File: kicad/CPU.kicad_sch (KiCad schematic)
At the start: 0 parts

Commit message: [kicad] Added HSE + HSE calculation
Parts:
- added C10, C11: 5pF, symbol Device:C_Small
- added R13: 50, symbol Device:R_Small
- added U5: STM32F303CBTx, Package_QFP:LQFP-48_7x7mm_P0.5mm, symbol MCU_ST_STM32F3:STM32F303CBTx
- added X1: 8 MHz, symbol Device:Crystal_Small
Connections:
- new net: C11.2, R13.1, X1.1
- new net: R13.2, U5.6 (PF1)
- new net: C10.2, U5.5 (PF0), X1.2
- new net: U5.23 (VSS), U5.35 (VSS), U5.47 (VSS)
- new net GND: C10.1, C11.1
- new net USB_DM: U5.32 (PA11)
- new net USB_DP: U5.33 (PA12)
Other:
- note added: "1. Load capacitance: (Cl-Cs)/2 = Cl1 = Cl2 2. Gain margin: gmcrit = 4×ESR×(2πF)×(C0+CL)=0.5 mA/V 3. Rext: 1/(2πFCl2) = 53 Ohm 4. Gain margin: Becomes 0.87 mA/V"

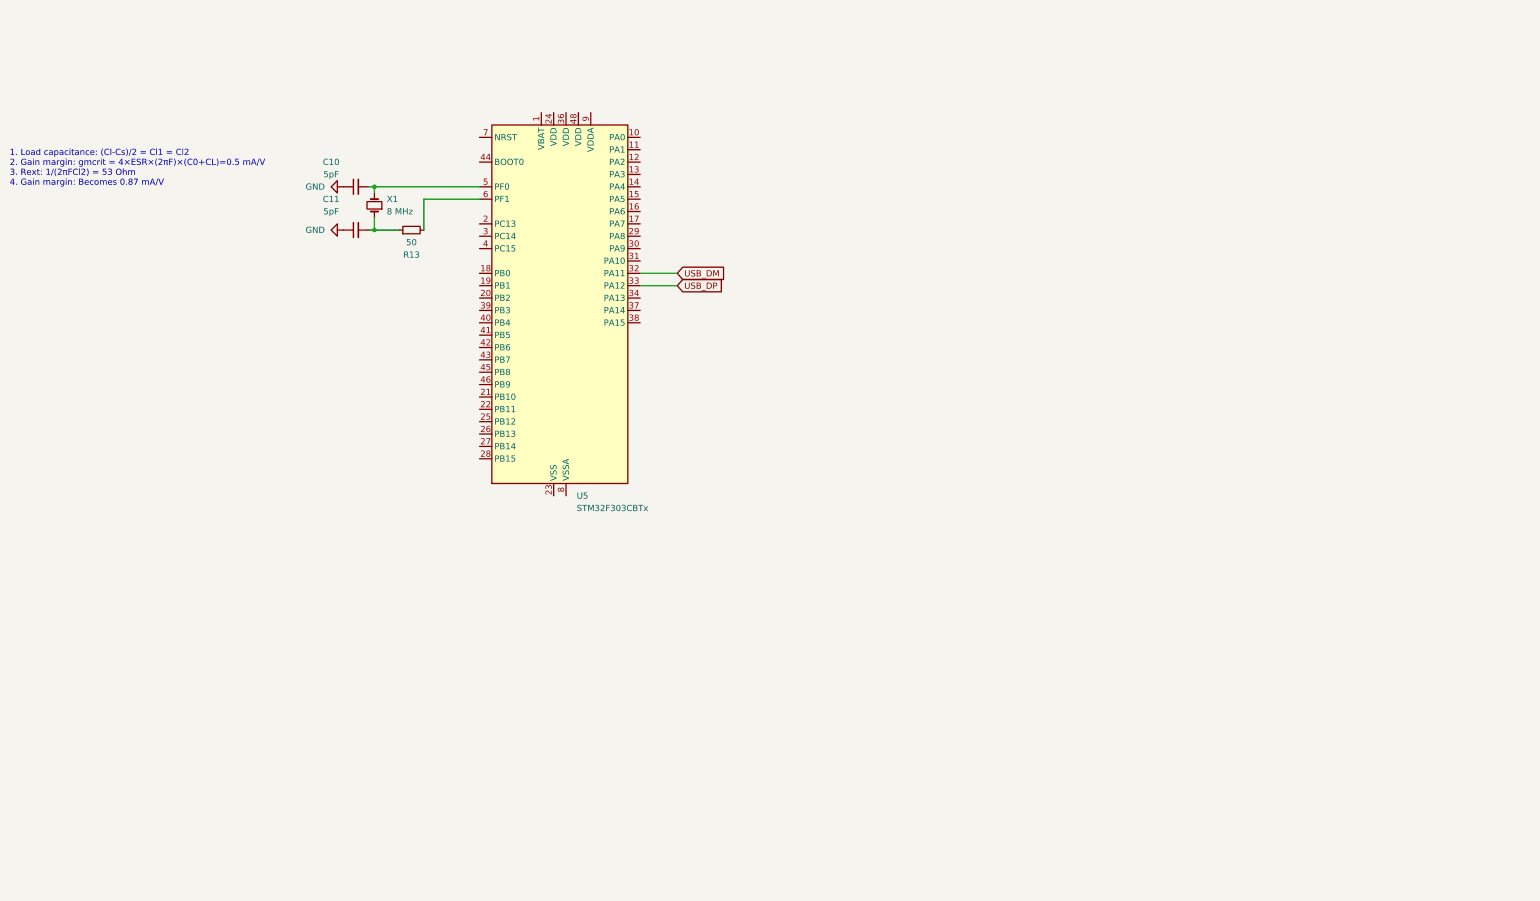
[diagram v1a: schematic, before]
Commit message: [kicad] BOOT0 pin done + SWD interface done
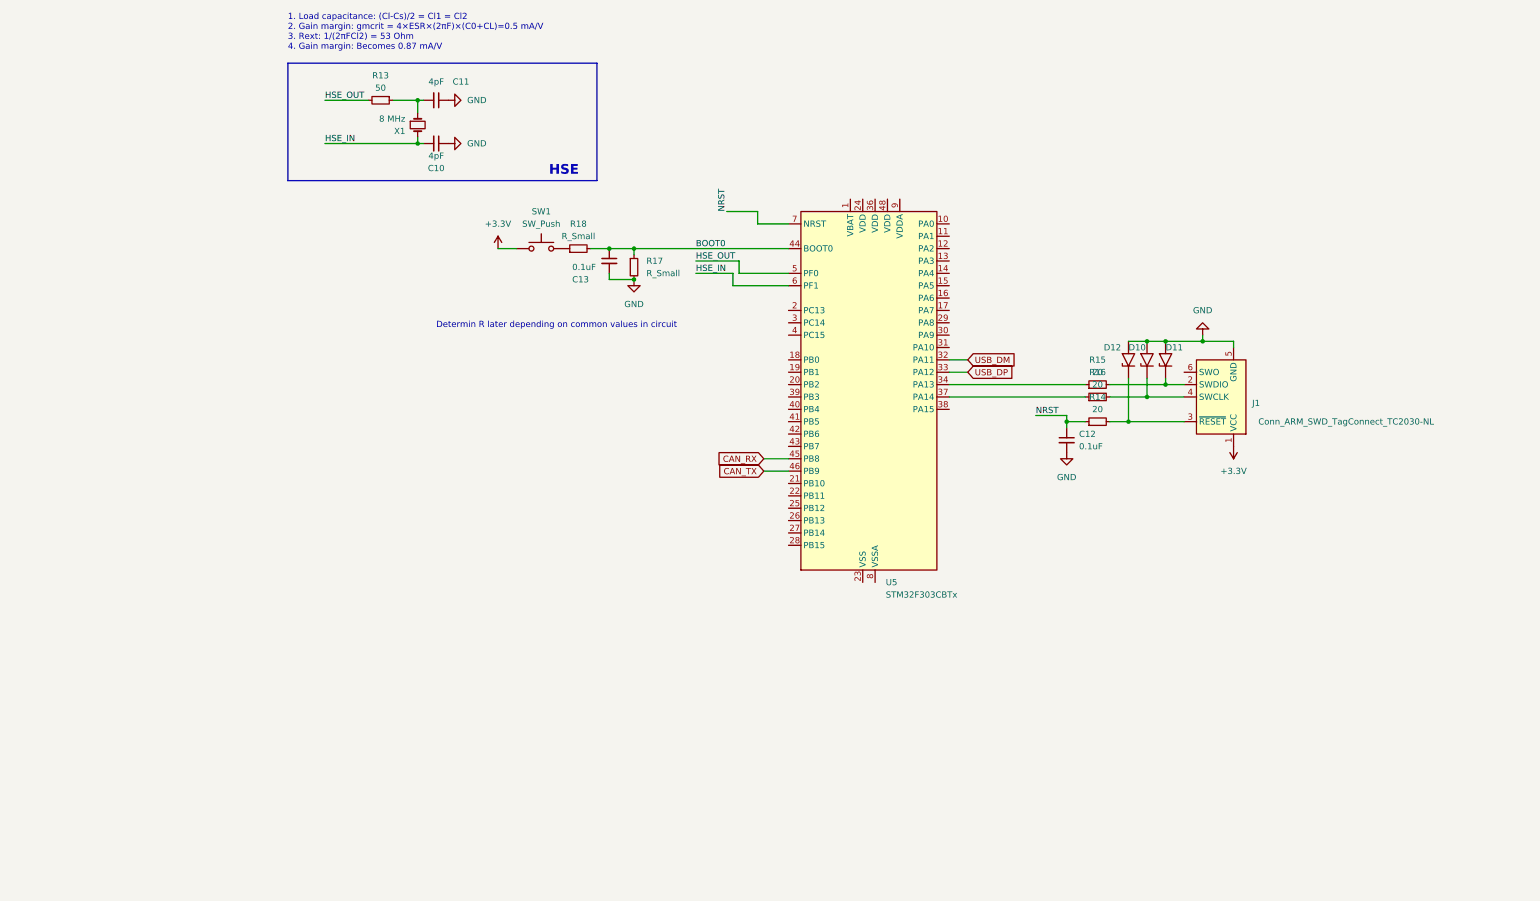
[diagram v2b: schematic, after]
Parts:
- added C12, C13: 0.1uF, symbol Device:C_Small
- added D10, D11, D12: SMAJ13A, Diode_SMD:D_SMA, symbol Diode:SMAJ13A
- added J1: Conn_ARM_SWD_TagConnect_TC2030-NL, Connector:Tag-Connect_TC2030-IDC-NL_2x03_P1.27mm_Vertical, symbol Connector:Conn_ARM_SWD_TagConnect_TC2030-NL
- added R14, R15, R16: 20, symbol Device:R_Small
- added R17, R18: R_Small, symbol Device:R_Small
- added SW1: SW_Push, symbol Switch:SW_Push
- C10, C11: value 5pF -> 4pF
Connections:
- net GND: now also C12.2, C13.2, D10.2 (A2), D11.2 (A2), D12.2 (A2), J1.5 (GND), R17.2
- net HSE_IN: now reaches U5.6 (PF1)
- net HSE_IN: now also C10.2, X1.2; no longer R13.2
- net at U5.34 (PA13): now also R15.1
- net at U5.37 (PA14): now also R16.1
- net BOOT0: now reaches U5.44 (BOOT0)
- net BOOT0: now also C13.1, R17.1, R18.2
- net CAN_RX: now reaches U5.45 (PB8)
- net CAN_TX: now reaches U5.46 (PB9)
- net NRST: now reaches U5.7 (NRST)
- net NRST: now also C12.1, R14.1
- new net: R18.1, SW1.2
- new net: D12.1 (A1), J1.3 (~{RESET}), R14.2
- new net: D11.1 (A1), J1.2 (SWDIO), R15.2
- new net: D10.1 (A1), J1.4 (SWCLK), R16.2
- new net +3.3V: J1.1 (VCC), SW1.1
- new net HSE_OUT: R13.2, U5.5 (PF0)
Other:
- note added: "Determin R later depending on common values in circuit"
- moved on the sheet: C10, C11, R13, U5, X1

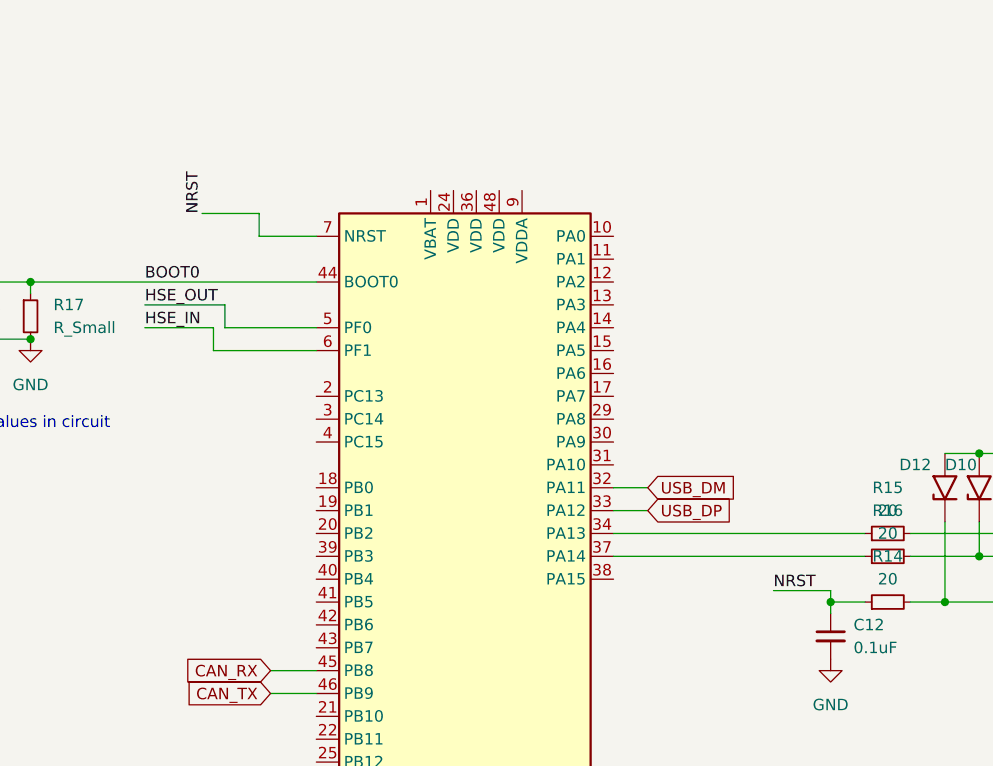
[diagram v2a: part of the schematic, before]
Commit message: [kicad] Added resistive bridge + virtual star for back-EMF meausrement, [cubemx] Added cubemx configuration file |TODO| Check ADC-DMA, ADC-CMP and interrupt with ADC functions, ADC-DMA
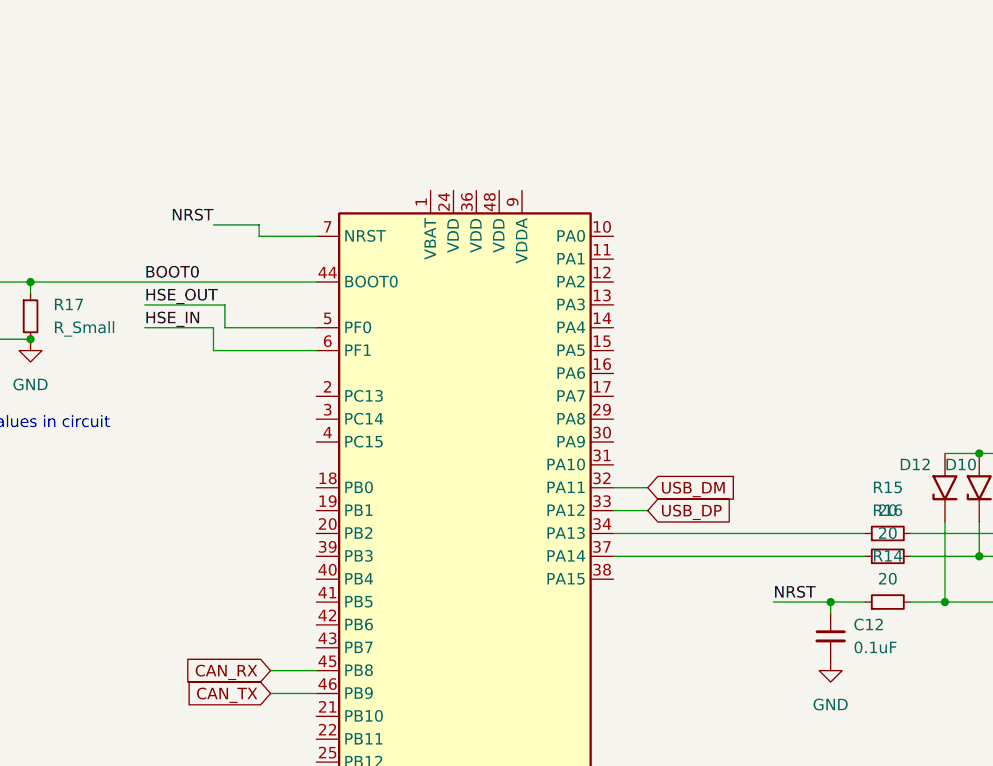
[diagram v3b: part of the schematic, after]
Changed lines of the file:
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@@
   (junction (at 80.01 63.5) (diameter 0) (color 0 0 0 0)
   )
-  (wire (pts (xy 104.14 55.88) (xy 110.49 55.88))
+  (wire (pts (xy 105.41 57.15) (xy 110.49 57.15))
     (stroke (width 0) (type default))
   )
@@
     (stroke (width 0) (type default))
   )
-  (wire (pts (xy 110.49 55.88) (xy 110.49 58.42))
+  (wire (pts (xy 110.49 57.15) (xy 110.49 58.42))
     (stroke (width 0) (type default))
   )
@@
     (stroke (width 0) (type default))
   )
-  (wire (pts (xy 173.99 97.79) (xy 173.99 99.06))
-    (stroke (width 0) (type default))
-  )
   (wire (pts (xy 106.68 68.58) (xy 116.84 68.58))
     (stroke (width 0) (type default))
@@
     (stroke (width 0) (type default))
   )
-  (wire (pts (xy 167.64 97.79) (xy 173.99 97.79))
+  (wire (pts (xy 167.64 99.06) (xy 173.99 99.06))
     (stroke (width 0) (type default))
   )
@@
     (effects (font (size 1.27 1.27)) (justify left bottom))
   )
-  (label "NRST" (at 167.64 97.79 0) (fields_autoplaced)
+  (label "NRST" (at 167.64 99.06 0) (fields_autoplaced)
     (effects (font (size 1.27 1.27)) (justify left bottom))
   )
-  (label "NRST" (at 104.14 55.88 90) (fields_autoplaced)
-    (effects (font (size 1.27 1.27)) (justify left bottom))
+  (label "NRST" (at 105.41 57.15 180) (fields_autoplaced)
+    (effects (font (size 1.27 1.27)) (justify right bottom))
   )
   (global_label "USB_DM" (shape input) (at 153.67 86.36 0) (fields_autoplaced)

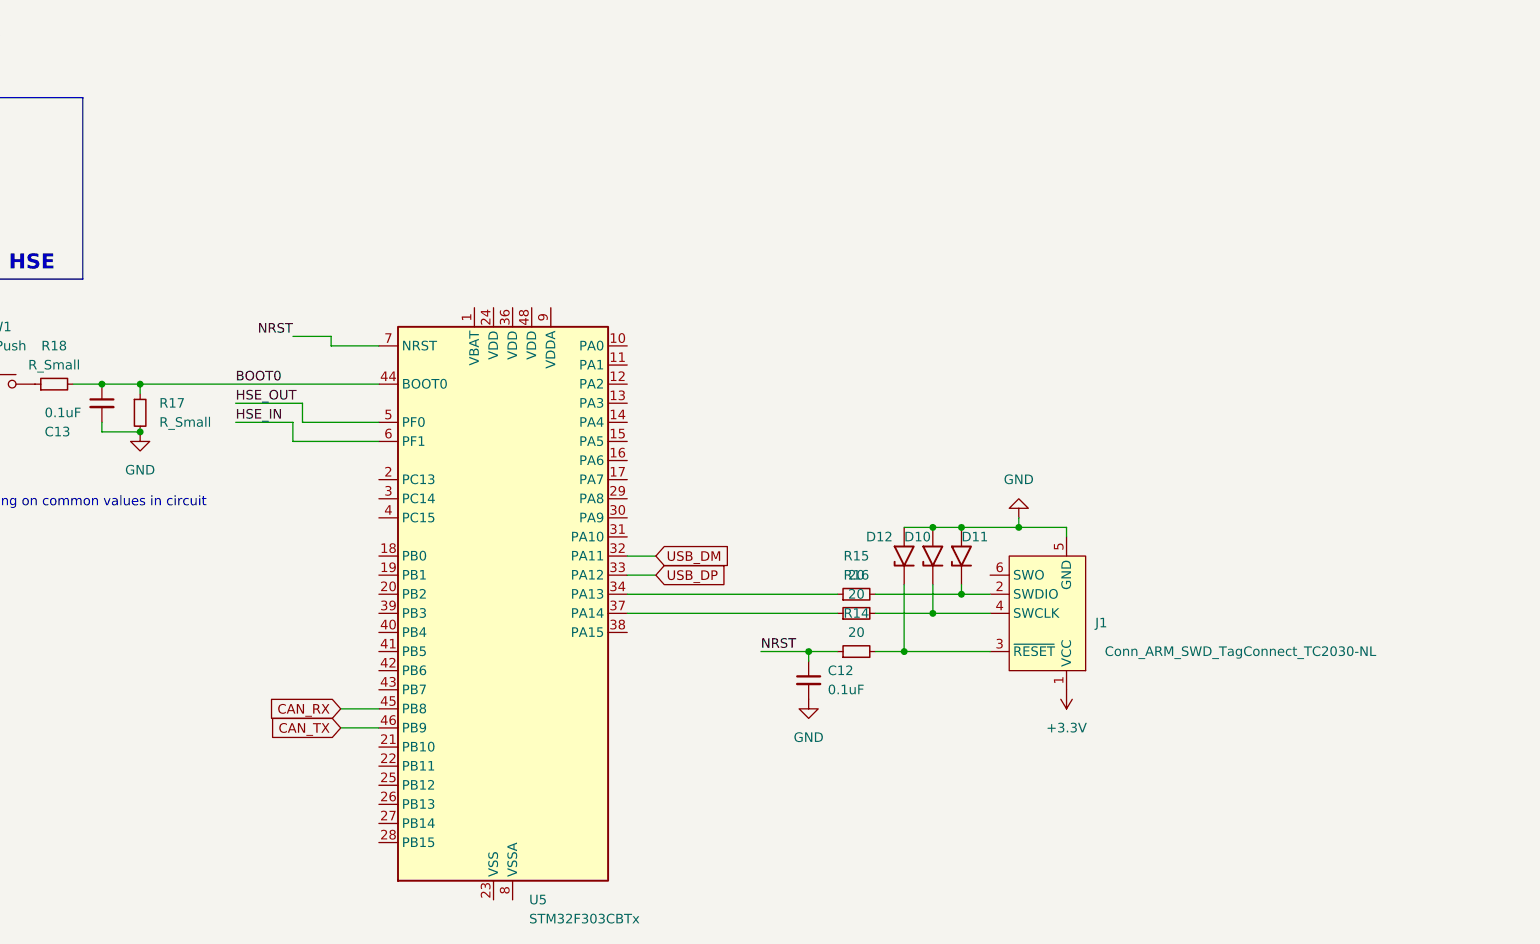
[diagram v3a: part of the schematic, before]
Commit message: [kicad] Added ADC_in, PWM_out labels as well as thermistor + battery management voltage divider | TODO: search for thermistor + CAN-circuit
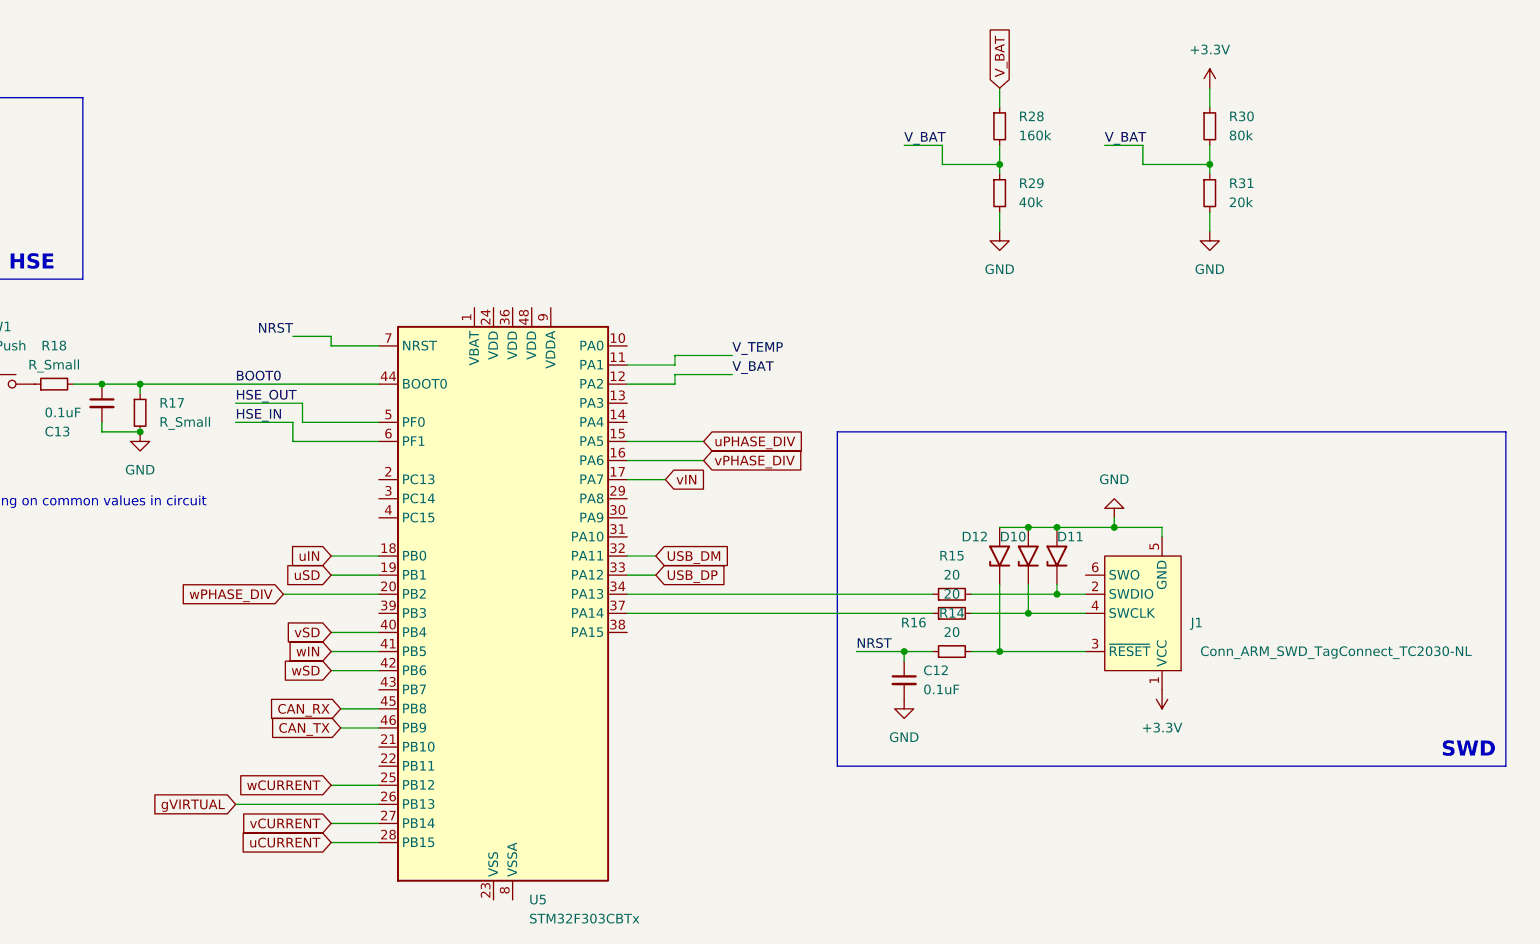
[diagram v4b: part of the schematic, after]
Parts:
- added R28: 160k, symbol Device:R_Small
- added R29: 40k, symbol Device:R_Small
- added R30: 80k, symbol Device:R_Small
- added R31: 20k, symbol Device:R_Small
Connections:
- net +3.3V: now also R30.1
- net GND: now also R29.2, R31.2
- net V_TEMP: now reaches U5.11 (PA1)
- net V_BAT: now reaches U5.12 (PA2)
- net V_BAT: now also R28.1, R28.2, R29.1, R30.2, R31.1
- net uPHASE_DIV: now reaches U5.15 (PA5)
- net vPHASE_DIV: now reaches U5.16 (PA6)
- net vIN: now reaches U5.17 (PA7)
- net uIN: now reaches U5.18 (PB0)
- net uSD: now reaches U5.19 (PB1)
- net wPHASE_DIV: now reaches U5.20 (PB2)
- net wCURRENT: now reaches U5.25 (PB12)
- net gVIRTUAL: now reaches U5.26 (PB13)
- net vCURRENT: now reaches U5.27 (PB14)
- net uCURRENT: now reaches U5.28 (PB15)
- net vSD: now reaches U5.40 (PB4)
- net wIN: now reaches U5.41 (PB5)
- net wSD: now reaches U5.42 (PB6)
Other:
- moved on the sheet: C12, D10, D11, D12, J1, R14, R15, R16
